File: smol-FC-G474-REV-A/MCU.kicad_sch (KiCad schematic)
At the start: 41 parts, among them J1 USB-C-16P, SW1 BOOT, U1 STM32G474RETx, U2 USBLC6-2P6, Y1 8MHz

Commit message: Attached footprints and finalized schematic.
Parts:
- 3V3_CORE1, GND2, NRST1, SWCLK1, SWDIO1: footprint (none) -> TestPoint:TestPoint_Pad_D1.0mm; now left out of the parts list
- C1, C10, C11, C12, C13, C14, C2, C3, C4, C5, C6, C7, C8, C9: footprint (none) -> Capacitor_SMD:C_0402_1005Metric
- D1, D2, D3, D5: footprint (none) -> LED_SMD:LED_0603_1608Metric
- D4: footprint (none) -> ESDALC6V1-1U2:DIODE_ESDALC6V1-1U2
- J1: footprint (none) -> USB-C:SHOUHAN_TYPE-C_16PIN_2MD__073_
- R1, R10, R11, R12, R2, R3, R4, R5, R6, R7, R8, R9: footprint (none) -> Resistor_SMD:R_0402_1005Metric
- SW1: footprint (none) -> B3U-1000P:B3U-1000P
- U1: footprint (none) -> Package_QFP:LQFP-64_10x10mm_P0.5mm
- U2: footprint (none) -> Package_TO_SOT_SMD:SOT-666
- Y1: footprint (none) -> NX3225GD:XTAL_NX3225GD-8MHZ-STD-CRA-3
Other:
- title: smol-FC-G474 -> smol-FC-G474-REV-A
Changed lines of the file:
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@@
 	(paper "A4")
 	(title_block
-		(title "smol-FC-G474")
-		(date "2026-05-31")
-		(rev "0.7.0")
+		(title "smol-FC-G474-REV-A")
+		(date "2026-06-05")
+		(rev "0.9.3")
 		(company "Daniel Plewa")
 		(comment 1 "License: CERN-OHL-W v2")
 		(comment 2 "GitHub: https://github.com/Def12345678/smol-FC-G474-REV-A")
-		(comment 3 "BEC 5A/2A, 10V/2A | Baro, OSD Chip and 16MB blackbox")
+		(comment 3 "BEC 5A/3A, 10V/3A | Baro, OSD Chip and 16MB blackbox")
 		(comment 4 "Open source flight controller on STM32G4, 20x20 3.5mm hole")
 	)
@@
 			)
 		)
-		(property "Footprint" ""
+		(property "Footprint" "Resistor_SMD:R_0402_1005Metric"
 			(at 85.09 110.49 0)
 			(hide yes)
@@
 			)
 		)
-		(property "Footprint" ""
+		(property "Footprint" "Capacitor_SMD:C_0402_1005Metric"
 			(at 86.36 29.21 0)
 			(hide yes)
@@
 			)
 		)
-		(property "Footprint" ""
+		(property "Footprint" "B3U-1000P:B3U-1000P"
 			(at 261.62 87.63 0)
 			(hide yes)
@@
 			)
 		)
-		(property "Footprint" ""
+		(property "Footprint" "Capacitor_SMD:C_0402_1005Metric"
 			(at 205.74 66.04 0)
 			(hide yes)
@@
 			)
 		)
-		(property "Footprint" ""
+		(property "Footprint" "Resistor_SMD:R_0402_1005Metric"
 			(at 19.05 78.74 0)
 			(hide yes)
@@
 			)
 		)
-		(property "Footprint" ""
+		(property "Footprint" "Capacitor_SMD:C_0402_1005Metric"
 			(at 40.64 29.21 0)
 			(hide yes)
@@
 			)
 		)
-		(property "Footprint" ""
+		(property "Footprint" "NX3225GD:XTAL_NX3225GD-8MHZ-STD-CRA-3"
 			(at 105.41 152.4 0)
 			(hide yes)
@@
 		(body_style 1)
 		(exclude_from_sim no)
-		(in_bom yes)
+		(in_bom no)
 		(on_board yes)
 		(in_pos_files yes)
@@
 			)
 		)
-		(property "Footprint" ""
+		(property "Footprint" "TestPoint:TestPoint_Pad_D1.0mm"
 			(at 270.51 63.5 0)
 			(hide yes)
@@
 		(body_style 1)
 		(exclude_from_sim no)
-		(in_bom yes)
+		(in_bom no)
 		(on_board yes)
 		(in_pos_files yes)
@@
 			)
 		)
-		(property "Footprint" ""
+		(property "Footprint" "TestPoint:TestPoint_Pad_D1.0mm"
 			(at 265.43 55.88 0)
 			(hide yes)
@@
 			)
 		)
-		(property "Footprint" ""
+		(property "Footprint" "ESDALC6V1-1U2:DIODE_ESDALC6V1-1U2"
 			(at 245.11 100.33 0)
 			(hide yes)
@@
 			)
 		)
-		(property "Footprint" ""
+		(property "Footprint" "Capacitor_SMD:C_0402_1005Metric"
 			(at 97.79 158.75 0)
 			(hide yes)
@@
 			)
 		)
-		(property "Footprint" ""
+		(property "Footprint" "Capacitor_SMD:C_0402_1005Metric"
 			(at 29.21 29.21 0)
 			(hide yes)
@@
 			)
 		)
-		(property "Footprint" ""
+		(property "Footprint" "Capacitor_SMD:C_0402_1005Metric"
 			(at 88.9 92.71 0)
 			(hide yes)
@@
 			)
 		)
-		(property "Footprint" ""
+		(property "Footprint" "Resistor_SMD:R_0402_1005Metric"
 			(at 19.05 88.9 0)
 			(hide yes)
@@
 			)
 		)
-		(property "Footprint" ""
+		(property "Footprint" "Package_TO_SOT_SMD:SOT-666"
 			(at 77.216 138.811 0)
 			(hide yes)
@@
 			)
 		)
-		(property "Footprint" ""
+		(property "Footprint" "USB-C:SHOUHAN_TYPE-C_16PIN_2MD__073_"
 			(at 42.926 96.52 0)
 			(hide yes)
@@
 			)
 		)
-		(property "Footprint" ""
+		(property "Footprint" "LED_SMD:LED_0603_1608Metric"
 			(at 102.87 67.31 0)
 			(hide yes)
@@
 			)
 		)
-		(property "Footprint" ""
+		(property "Footprint" "Package_QFP:LQFP-64_10x10mm_P0.5mm"
 			(at 135.89 158.75 0)
 			(hide yes)
@@
 			)
 		)
-		(property "Footprint" ""
+		(property "Footprint" "LED_SMD:LED_0603_1608Metric"
 			(at 257.81 147.32 0)
 			(hide yes)
@@
 			)
 		)
-		(property "Footprint" ""
+		(property "Footprint" "Capacitor_SMD:C_0402_1005Metric"
 			(at 63.5 29.21 0)
 			(hide yes)
@@
 			)
 		)
-		(property "Footprint" ""
+		(property "Footprint" "Capacitor_SMD:C_0402_1005Metric"
 			(at 113.03 158.75 0)
 			(hide yes)
@@
 			)
 		)
-		(property "Footprint" ""
+		(property "Footprint" "Capacitor_SMD:C_0402_1005Metric"
 			(at 99.06 92.71 0)
 			(hide yes)
@@
 			)
 		)
-		(property "Footprint" ""
+		(property "Footprint" "Capacitor_SMD:C_0402_1005Metric"
 			(at 19.05 29.21 0)
 			(hide yes)
@@
 			)
 		)
-		(property "Footprint" ""
+		(property "Footprint" "Capacitor_SMD:C_0402_1005Metric"
 			(at 74.93 29.21 0)
 			(hide yes)
@@
 			)
 		)
-		(property "Footprint" ""
+		(property "Footprint" "Resistor_SMD:R_0402_1005Metric"
 			(at 257.81 135.89 0)
 			(hide yes)
@@
 			)
 		)
-		(property "Footprint" ""
+		(property "Footprint" "LED_SMD:LED_0603_1608Metric"
 			(at 93.98 67.31 0)
 			(hide yes)
@@
 			)
 		)
-		(property "Footprint" ""
+		(property "Footprint" "Resistor_SMD:R_0402_1005Metric"
 			(at 85.09 55.88 0)
 			(hide yes)
@@
 			)
 		)
-		(property "Footprint" ""
+		(property "Footprint" "Resistor_SMD:R_0402_1005Metric"
 			(at 67.31 153.67 0)
 			(hide yes)
@@
 			)
 		)
-		(property "Footprint" ""
+		(property "Footprint" "LED_SMD:LED_0603_1608Metric"
 			(at 85.09 67.31 0)
 			(hide yes)
@@
 			)
 		)
-		(property "Footprint" ""
+		(property "Footprint" "Resistor_SMD:R_0402_1005Metric"
 			(at 207.01 50.8 0)
 			(hide yes)
@@
 			)
 		)
-		(property "Footprint" ""
+		(property "Footprint" "Capacitor_SMD:C_0402_1005Metric"
 			(at 110.49 29.21 0)
 			(hide yes)
@@
 			)
 		)
-		(property "Footprint" ""
+		(property "Footprint" "Resistor_SMD:R_0402_1005Metric"
 			(at 252.73 100.33 0)
 			(hide yes)
@@
 		(body_style 1)
 		(exclude_from_sim no)
-		(in_bom yes)
+		(in_bom no)
 		(on_board yes)
 		(in_pos_files yes)
@@
 			)
 		)
-		(property "Footprint" ""
+		(property "Footprint" "TestPoint:TestPoint_Pad_D1.0mm"
 			(at 260.35 48.26 0)
 			(hide yes)
@@
 		(body_style 1)
 		(exclude_from_sim no)
-		(in_bom yes)
+		(in_bom no)
 		(on_board yes)
 		(in_pos_files yes)
@@
 			)
 		)
-		(property "Footprint" ""
+		(property "Footprint" "TestPoint:TestPoint_Pad_D1.0mm"
 			(at 267.97 59.69 0)
 			(hide yes)
@@
 			)
 		)
-		(property "Footprint" ""
+		(property "Footprint" "Resistor_SMD:R_0402_1005Metric"
 			(at 93.98 55.88 0)
 			(hide yes)
@@
 			)
 		)
-		(property "Footprint" ""
+		(property "Footprint" "Capacitor_SMD:C_0402_1005Metric"
 			(at 97.79 29.21 0)
 			(hide yes)
@@
 			)
 		)
-		(property "Footprint" ""
+		(property "Footprint" "Resistor_SMD:R_0402_1005Metric"
 			(at 63.5 153.67 0)
 			(hide yes)
@@
 		(body_style 1)
 		(exclude_from_sim no)
-		(in_bom yes)
+		(in_bom no)
 		(on_board yes)
 		(in_pos_files yes)
@@
 			)
 		)
-		(property "Footprint" ""
+		(property "Footprint" "TestPoint:TestPoint_Pad_D1.0mm"
 			(at 262.89 52.07 0)
 			(hide yes)
@@
 			)
 		)
-		(property "Footprint" ""
+		(property "Footprint" "Resistor_SMD:R_0402_1005Metric"
 			(at 85.09 120.65 0)
 			(hide yes)
@@
 			)
 		)
-		(property "Footprint" ""
+		(property "Footprint" "Resistor_SMD:R_0402_1005Metric"
 			(at 102.87 55.88 0)
 			(hide yes)
@@
 			)
 		)
-		(property "Footprint" ""
+		(property "Footprint" "Capacitor_SMD:C_0402_1005Metric"
 			(at 52.07 29.21 0)
 			(hide yes)

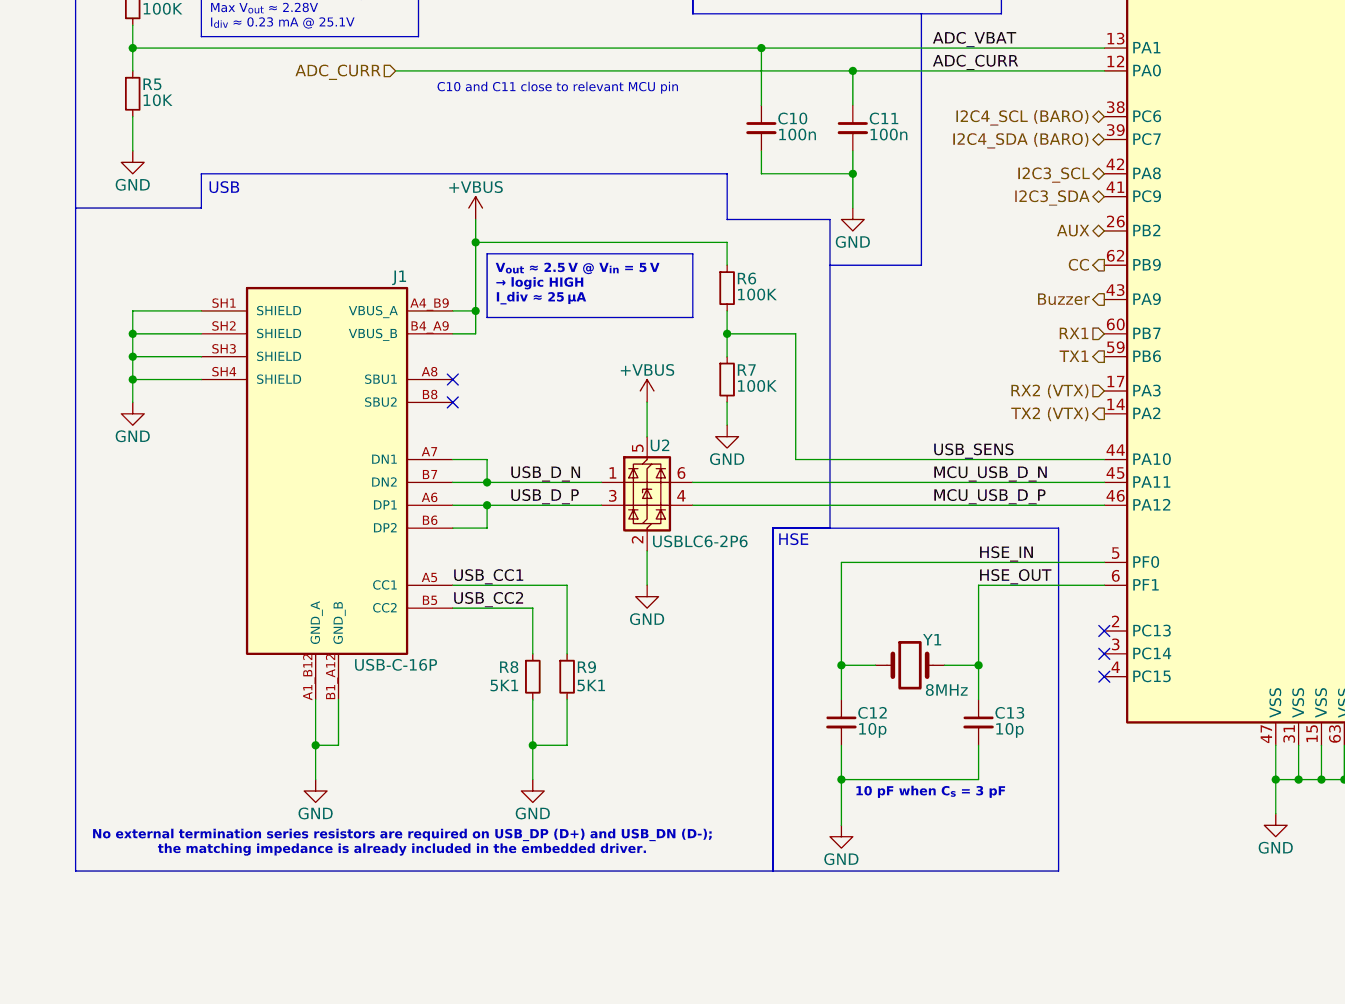
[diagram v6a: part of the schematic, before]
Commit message: Finalized schematic, added power mux
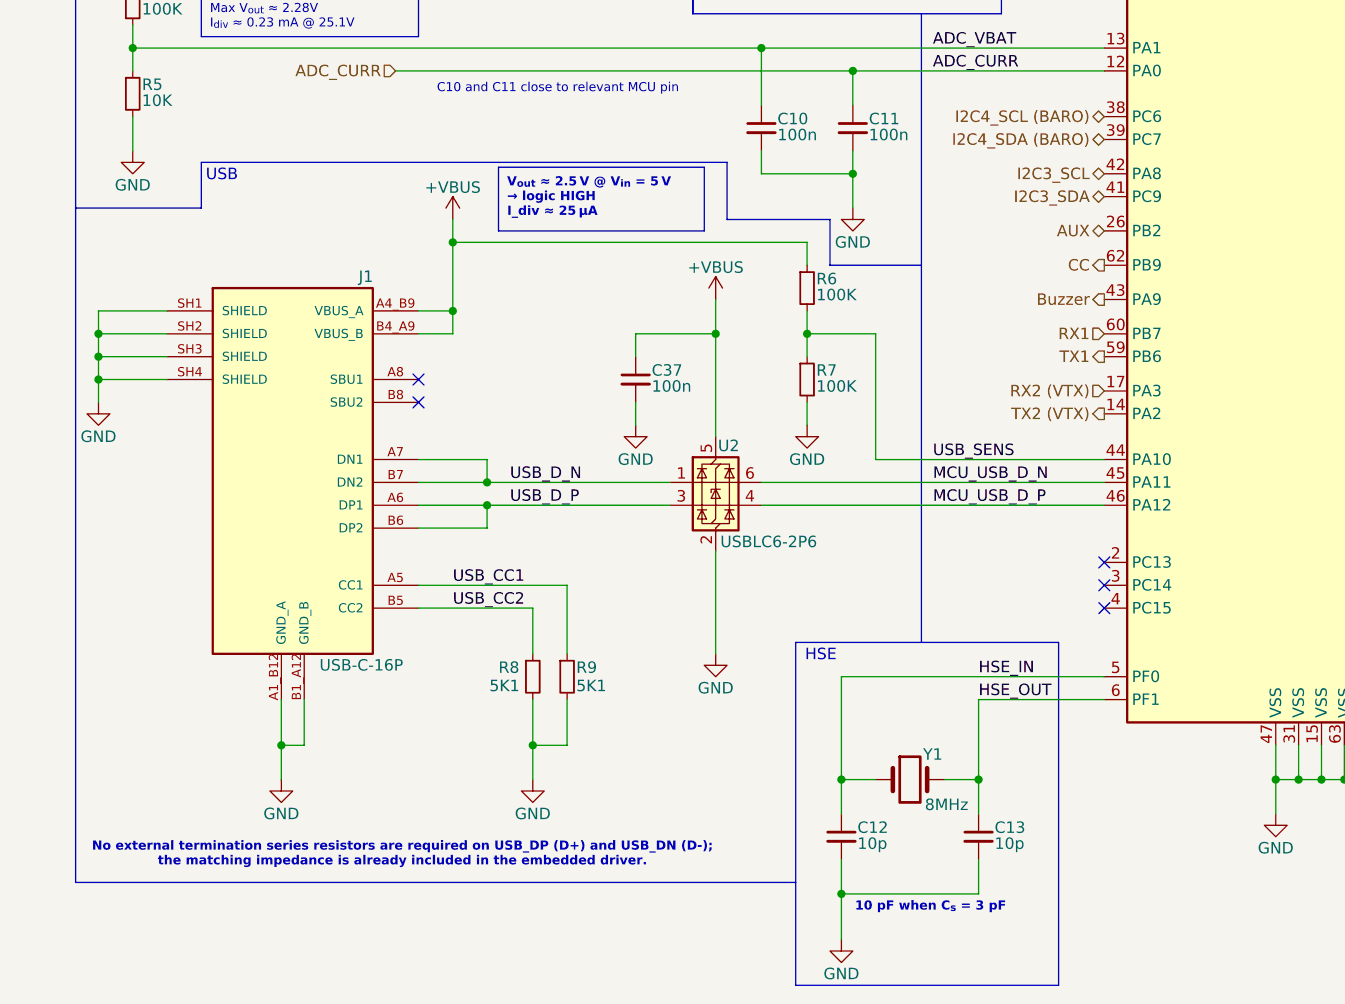
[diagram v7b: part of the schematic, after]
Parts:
- added C37: 100n, Capacitor_SMD:C_0402_1005Metric, symbol Device:C_Small
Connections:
- net +VBUS: now also C37.1
- net GND: now also C37.2
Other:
- moved on the sheet: C12, C13, J1, R6, R7, U2, Y1

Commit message: In progress PCB layout
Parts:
- removed C6: 10n, Capacitor_SMD:C_0402_1005Metric, symbol Device:C_Small
- removed C9: 1u, Capacitor_SMD:C_0402_1005Metric, symbol Device:C_Small
- removed D3: LED, LED_SMD:LED_0603_1608Metric, symbol Device:LED
- removed J1: USB-C-16P, USB-C:SHOUHAN_TYPE-C_16PIN_2MD__073_, symbol TYPE-C_16PIN_2MD__073_:TYPE-C_16PIN_2MD__073_
- removed NRST1: TestPoint, TestPoint:TestPoint_Pad_D1.0mm, symbol Connector:TestPoint
- removed R11: 10K, Resistor_SMD:R_0402_1005Metric, symbol Device:R_Small
- removed R3: 1K, Resistor_SMD:R_0402_1005Metric, symbol Device:R_Small
- added USB1: TYPE-C 16P QTWT, USB-C-SMD:USB-TYPE-C-SMD_TYPE-C-16P-QTWT, symbol USB-C_SMD:TYPE-C16PQTWT
- R1, R2: value 1K -> 1k
- R10: renamed from R9; value 5K1 -> 5.1k
- R3: renamed from R4; value 100K -> 100k
- R4: renamed from R5; value 10K -> 10k
- R5: renamed from R10; value 10K -> 10k
- R6, R7: value 100K -> 100k
- R8: renamed from R12; value 1K -> 1k
- R9: renamed from R8; value 5K1 -> 5.1k
- SW1: footprint B3U-1000P:B3U-1000P -> B3U-1000P:KEY-SMD_B3U-1000PM
- renumbered C11 to C10, C37 to C11, C7 to C6, C8 to C7, C14 to C8, C10 to C9, D4 to D3, D5 to D4, GND2 to GND1
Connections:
- net +VBUS: now also USB1.A4 (VBUS), USB1.A9 (VBUS)
- net GND: now also USB1.0 (EH), USB1.A1 (GND), USB1.A12 (GND)
- net USB_CC1: now also USB1.B5 (CC2)
- net USB_CC2: now also USB1.A5 (CC1)
- net USB_D_N: now also USB1.A7 (DN1), USB1.B7 (DN2)
- net USB_D_P: now also USB1.A6 (DP1), USB1.B6 (DP2)
- net LED_A: no longer names the net of U1.22 (PC4)
- no-connect marks 6 -> 7
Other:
- note added: "Blue, Green"
- note added: "C14 close to relevant MCU pin"
- note added: "VDDA and VREF shares decoupling pins."
- note removed: "Blue, Green, Amber"
- note removed: "C36 close to relevant MCU pin"
- moved on the sheet: C6, C7, C8, D1, D2, GND1, R1, R2
